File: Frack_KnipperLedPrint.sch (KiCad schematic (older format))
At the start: 14 parts, among them J1 Conn_01x01, J2 Conn_01x01, Q1 BC547, Q2 BC547

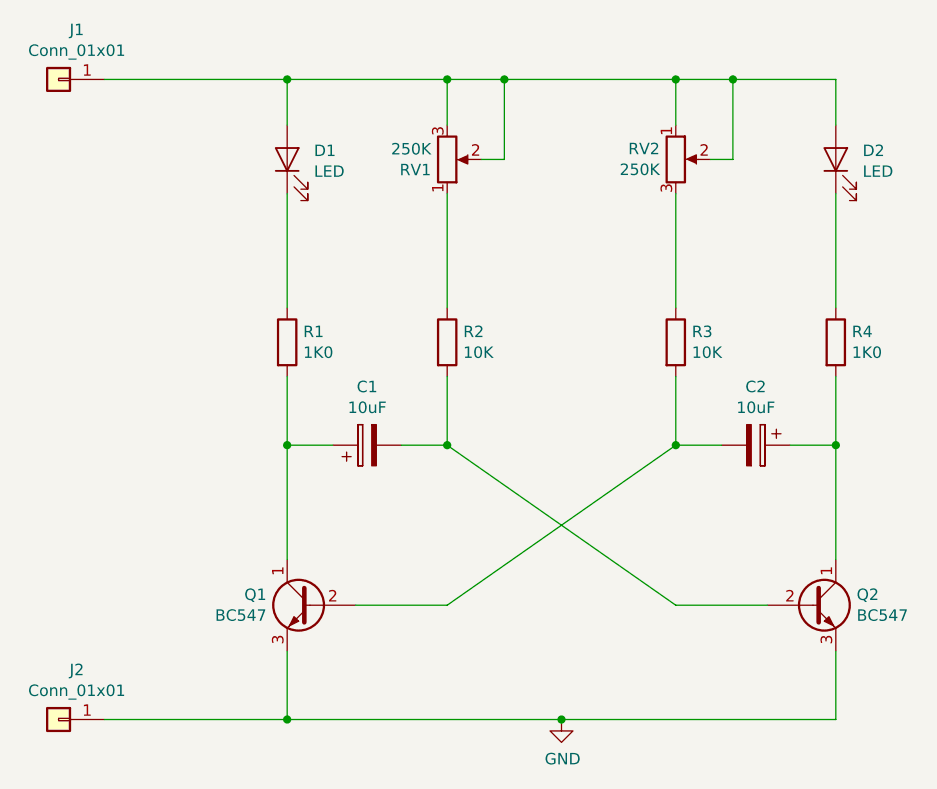
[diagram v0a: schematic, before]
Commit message: Annotations and render
Changed annotations to match old design
Added 3d model of potentiometer
Added render images of pcb
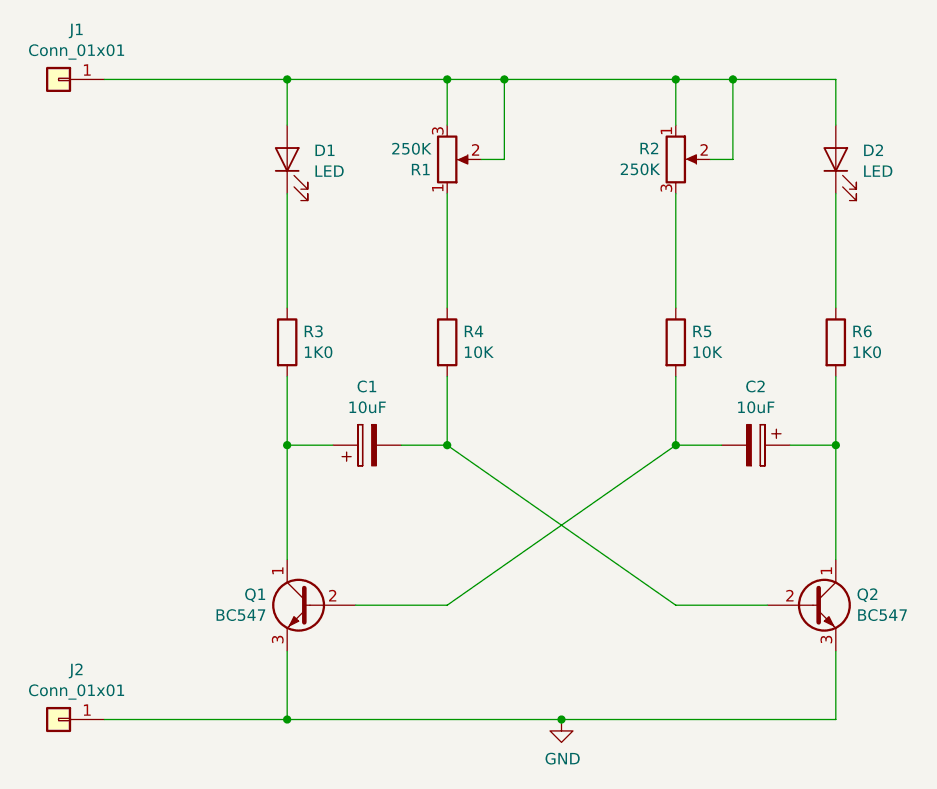
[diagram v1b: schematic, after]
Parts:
- R1: renamed from RV1; footprint Potentiometer_THT:Potentiometer_Piher_PT-6-V_Vertical -> Custom_parts:Potentiometer_Piher_PT-6-V_Vertical
- R2: renamed from RV2; footprint Potentiometer_THT:Potentiometer_Piher_PT-6-V_Vertical -> Custom_parts:Potentiometer_Piher_PT-6-V_Vertical
- renumbered R1 to R3, R2 to R4, R3 to R5, R4 to R6
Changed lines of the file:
@@
 $EndDescr
 $Comp
-L Device:R R1
+L Device:R R3
 U 1 1 5BF43F84
 P 3700 2750
-F 0 "R1" H 3770 2796 50  0000 L CNN
+F 0 "R3" H 3770 2796 50  0000 L CNN
 F 1 "1K0" H 3770 2705 50  0000 L CNN
 F 2 "Resistor_THT:R_Axial_DIN0207_L6.3mm_D2.5mm_P10.16mm_Horizontal" V 3630 2750 50  0001 C CNN
@@
 $EndComp
 $Comp
-L Device:R R3
+L Device:R R5
 U 1 1 5BF4407B
 P 5400 2750
-F 0 "R3" H 5470 2796 50  0000 L CNN
+F 0 "R5" H 5470 2796 50  0000 L CNN
 F 1 "10K" H 5470 2705 50  0000 L CNN
 F 2 "Resistor_THT:R_Axial_DIN0207_L6.3mm_D2.5mm_P10.16mm_Horizontal" V 5330 2750 50  0001 C CNN
@@
 $EndComp
 $Comp
-L Device:R_POT RV1
+L Device:R_POT R1
 U 1 1 5BF4410D
 P 4400 1950
-F 0 "RV1" H 4330 1996 50  0000 R CNN
+F 0 "R1" H 4330 1996 50  0000 R CNN
 F 1 "250K" H 4330 1905 50  0000 R CNN
-F 2 "Potentiometer_THT:Potentiometer_Piher_PT-6-V_Vertical" H 4400 1950 50  0001 C CNN
+F 2 "Custom_parts:Potentiometer_Piher_PT-6-V_Vertical" H 4400 1950 50  0001 C CNN
 F 3 "~" H 4400 1950 50  0001 C CNN
 	1    4400 1950
@@
 $EndComp
 $Comp
-L Device:R_POT RV2
+L Device:R_POT R2
 U 1 1 5BF44158
 P 5400 1950
-F 0 "RV2" H 5330 1996 50  0000 R CNN
+F 0 "R2" H 5330 1996 50  0000 R CNN
 F 1 "250K" H 5330 1905 50  0000 R CNN
-F 2 "Potentiometer_THT:Potentiometer_Piher_PT-6-V_Vertical" H 5400 1950 50  0001 C CNN
+F 2 "Custom_parts:Potentiometer_Piher_PT-6-V_Vertical" H 5400 1950 50  0001 C CNN
 F 3 "~" H 5400 1950 50  0001 C CNN
 	1    5400 1950
@@
 $EndComp
 $Comp
-L Device:R R2
+L Device:R R4
 U 1 1 5BF44448
 P 4400 2750
-F 0 "R2" H 4470 2796 50  0000 L CNN
+F 0 "R4" H 4470 2796 50  0000 L CNN
 F 1 "10K" H 4470 2705 50  0000 L CNN
 F 2 "Resistor_THT:R_Axial_DIN0207_L6.3mm_D2.5mm_P10.16mm_Horizontal" V 4330 2750 50  0001 C CNN
@@
 $EndComp
 $Comp
-L Device:R R4
+L Device:R R6
 U 1 1 5BF444A9
 P 6100 2750
-F 0 "R4" H 6170 2796 50  0000 L CNN
+F 0 "R6" H 6170 2796 50  0000 L CNN
 F 1 "1K0" H 6170 2705 50  0000 L CNN
 F 2 "Resistor_THT:R_Axial_DIN0207_L6.3mm_D2.5mm_P10.16mm_Horizontal" V 6030 2750 50  0001 C CNN
